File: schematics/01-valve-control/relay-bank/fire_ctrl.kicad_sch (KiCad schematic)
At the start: 7 parts, among them J601 VALVE, K601 SPST Relay, Q601 BSS138

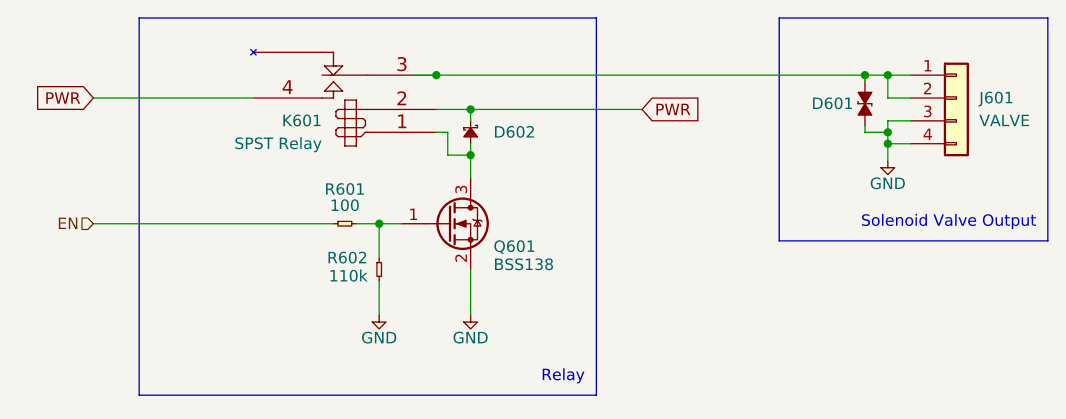
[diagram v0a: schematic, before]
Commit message: Relay bank changes for manufacture
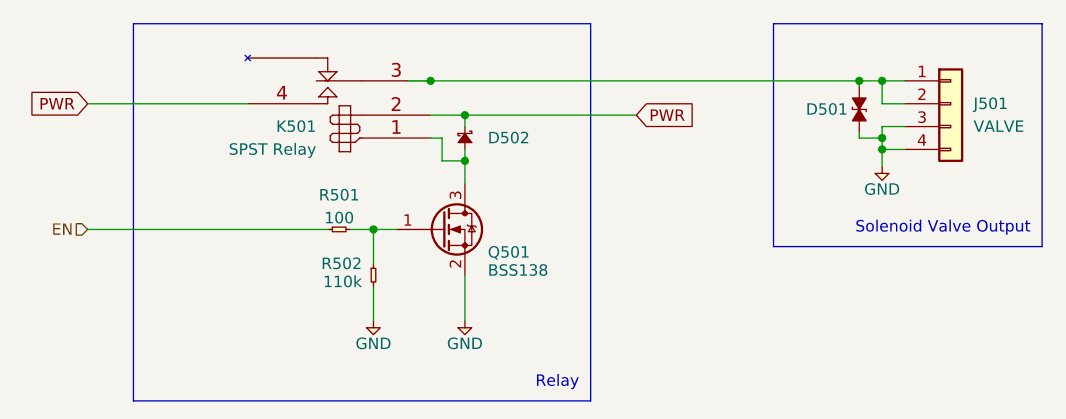
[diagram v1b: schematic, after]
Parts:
- D502: renamed from D602; Farnell (none) -> 3527901
- J501: renamed from J601; Farnell (none) -> 2820686
- K501: renamed from K601; Farnell (none) -> 1863384
- Q501: renamed from Q601; Farnell (none) -> 2053833
- R501: renamed from R601; Farnell (none) -> 2331443
- R502: renamed from R602; Farnell (none) -> 2059181
- renumbered D601 to D501
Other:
- moved on the sheet: D501, D502, J501, K501, Q501, R501, R502
